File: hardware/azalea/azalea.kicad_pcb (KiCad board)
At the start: 2 copper layers, 73.7 x 55.9 mm, 86 parts, among them J1 NEIGHBOR1, J2 NEIGHBOR2, J3 USB-MICRO-B-SHIELDED, J4 USB-MICRO-B-SHIELDED, J5 JTAG, J6 RTC, J7 BONUS_ROW, SW1 DFU, SW2 RESET, U1 LPC4330FBD144, U2 W25Q16DV, U3 AP7333, U4 IP4220CZ6, U5 NX5P2553GV, X1 XTAL4PIN, X2 RTC_XTAL

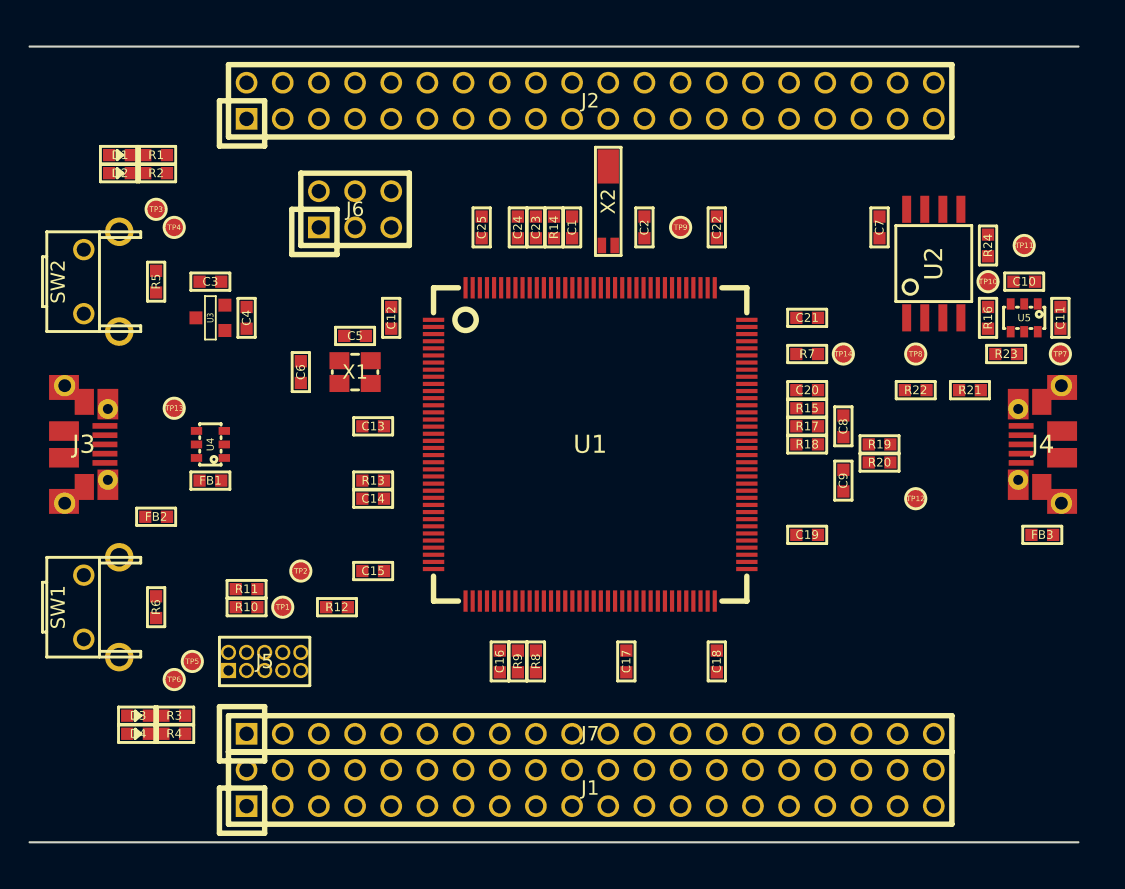
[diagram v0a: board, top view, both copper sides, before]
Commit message: azalea: added mounting holes
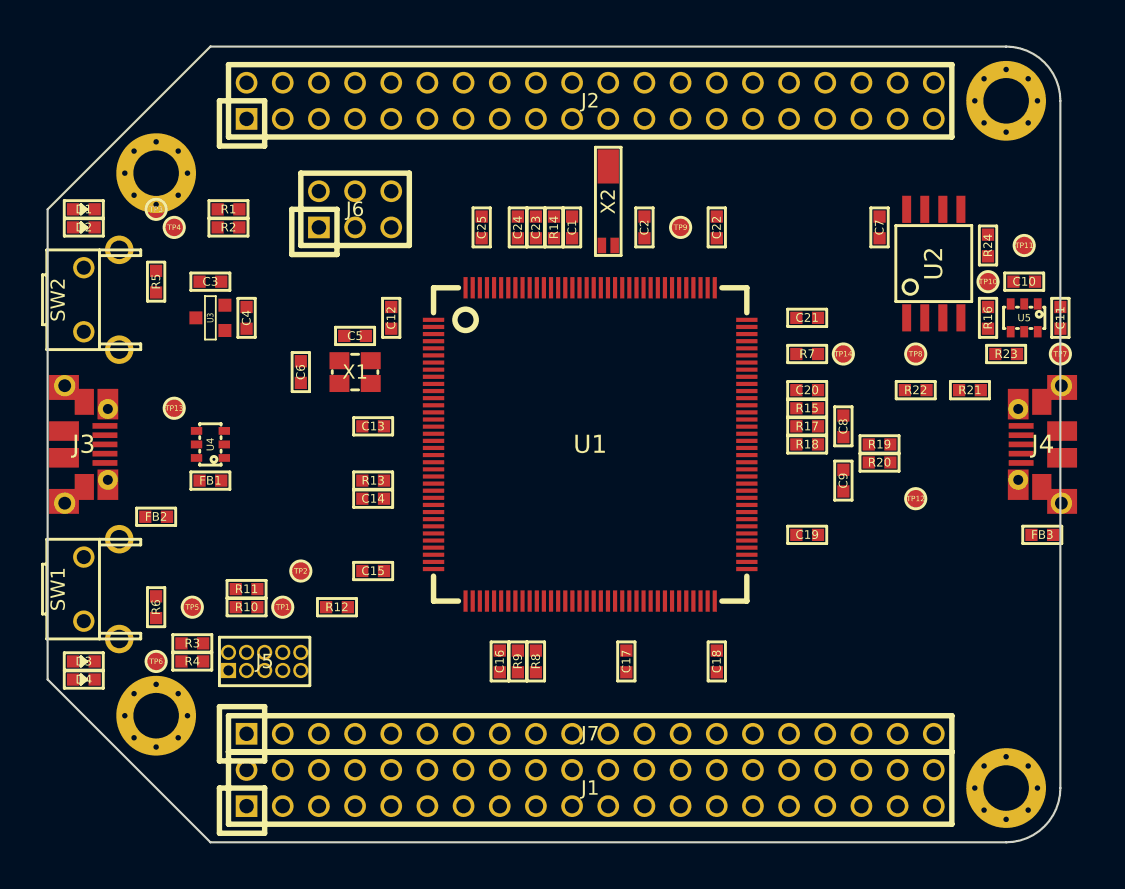
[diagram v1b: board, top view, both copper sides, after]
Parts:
- added MH1: MOUNTING_HOLE, gsg-modules:HOLE126MIL-COPPER, F.Cu at (111.8, 78.7)
- added MH2: MOUNTING_HOLE, gsg-modules:HOLE126MIL-COPPER, F.Cu at (111.8, 116.8)
- added MH3: MOUNTING_HOLE, gsg-modules:HOLE126MIL-COPPER, F.Cu at (171.4, 121.9)
- added MH4: MOUNTING_HOLE, gsg-modules:HOLE126MIL-COPPER, F.Cu at (171.4, 73.7)
- moved R1 6.35 mm to (116.8, 81.3)
- moved R2 6.35 mm to (116.8, 82.5)
- moved D3 5.39 mm to (106.7, 113.0)
- moved D4 5.39 mm to (106.7, 114.3)
- moved R3 5.24 mm to (114.3, 111.8)
- moved R4 5.24 mm to (114.3, 113.0)
- moved D1 4.58 mm to (106.7, 81.3)
- moved D2 4.58 mm to (106.7, 82.5)
- moved TP5 3.81 mm to (114.3, 109.2)
- moved TP6 1.80 mm to (111.8, 113.0)
- moved SW1 1.27 mm to (106.7, 108.0)
- moved SW2 1.27 mm to (106.7, 87.6)
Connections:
- net Net-(R10-Pad2) renamed /DBGEN
- net Net-(TP2-Pad1) renamed /TRST
- C1 pad 1: /RTCX1 -> /RTCX2
- C2 pad 1: /RTCX2 -> /RTCX1
- X2 pad 1: /RTCX1 -> /RTCX2
- X2 pad 2: /RTCX2 -> /RTCX1
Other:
- board size 73.7 x 55.9 mm -> 71.1 x 55.9 mm

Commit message: azalea: PCB shape
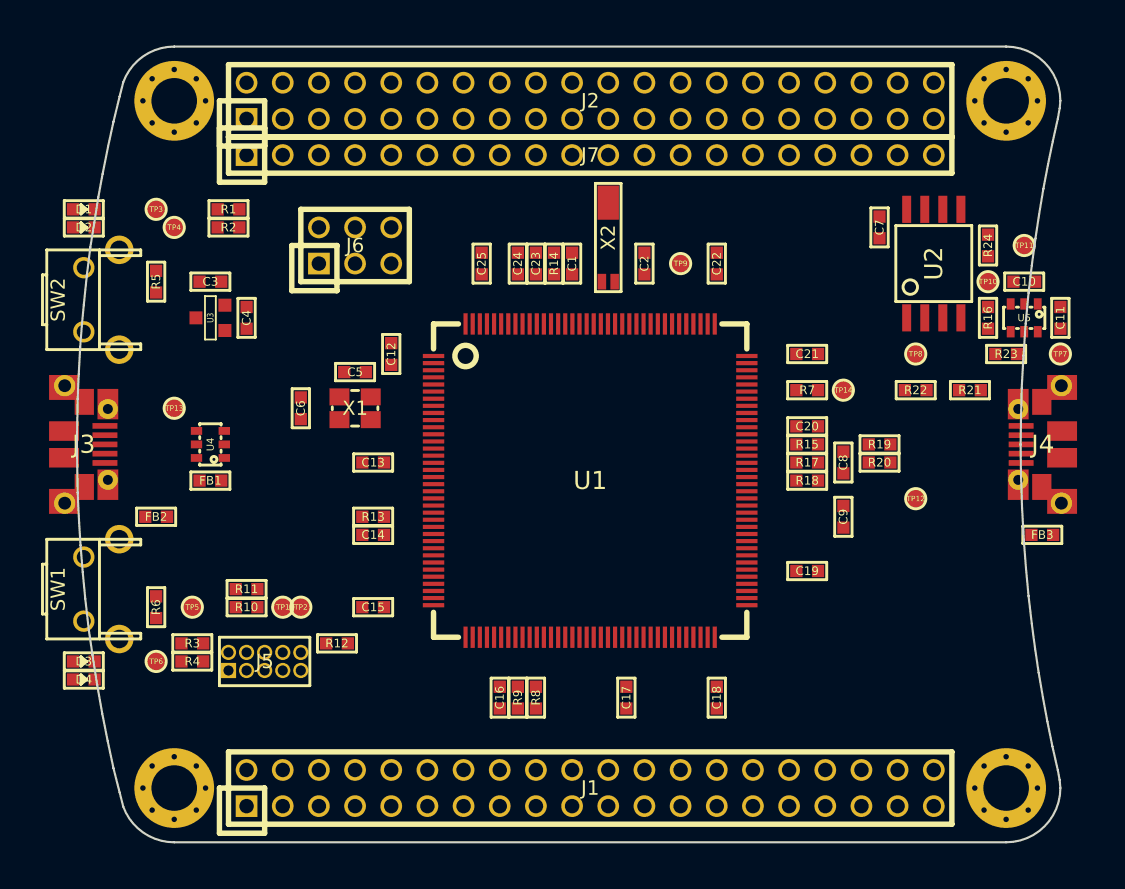
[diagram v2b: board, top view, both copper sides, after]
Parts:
- moved J7 40.6 mm to (142.2, 77.5)
- moved MH1 5.24 mm to (113.0, 73.7)
- moved MH2 5.24 mm to (113.0, 121.9)
- moved C1 2.54 mm to (141.0, 85.1)
- moved C13 2.54 mm to (127.0, 99.1)
- moved C14 2.54 mm to (127.0, 104.1)
- moved C19 2.54 mm to (157.5, 106.7)
- moved C2 2.54 mm to (146.1, 85.1)
- moved C22 2.54 mm to (151.1, 85.1)
- moved C23 2.54 mm to (138.4, 85.1)
- moved C24 2.54 mm to (137.2, 85.1)
- moved C25 2.54 mm to (134.6, 85.1)
- moved C6 2.54 mm to (121.9, 95.2)
- moved C8 2.54 mm to (160.0, 99.1)
- moved C9 2.54 mm to (160.0, 102.9)
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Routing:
- net /P1_10: track 0.00 -> 0.74 mm
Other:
- board size 71.1 x 55.9 mm -> 69.1 x 55.9 mm
- net class Default: clearance 0.2 -> 0.2032; trace_width 0.25 -> 0.2032; via_dia 0.6 -> 0.635; via_drill 0.4 -> 0.381
- rule trace_clearance: 0.2 -> 0.2032
- rule trace_min: 0.2 -> 0.2032
- rule via_min_drill: 0.3 -> 0.2032
- rule via_min_size: 0.4 -> 0.508

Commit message: azalea: made PCB slightly longer and narrower, mounting holes assymmetrical
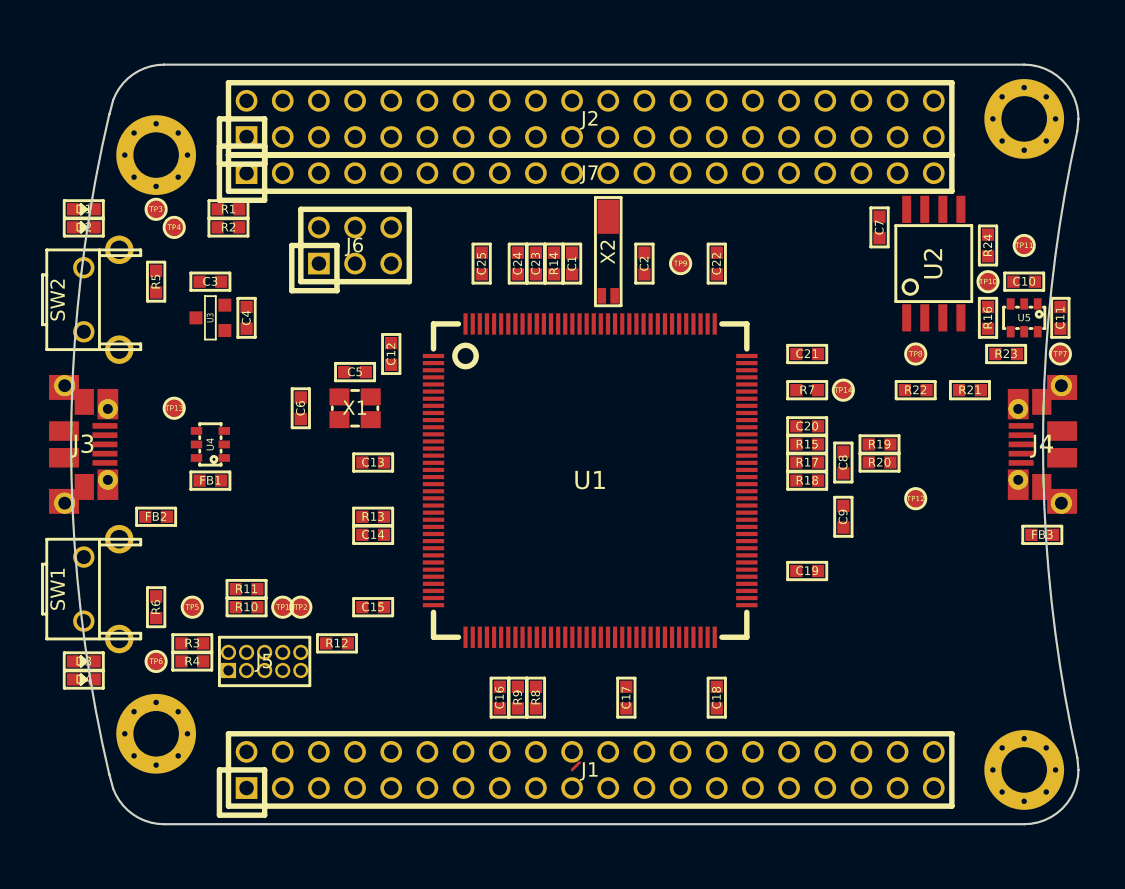
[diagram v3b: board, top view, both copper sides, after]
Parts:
- moved MH1 4.02 mm to (111.8, 77.5)
- moved MH2 4.02 mm to (111.8, 118.1)
- moved MH4 1.80 mm to (172.7, 74.9)
- moved MH3 1.80 mm to (172.7, 120.7)
- moved J2 1.27 mm to (142.2, 74.9)
- moved J1 1.27 mm to (142.2, 120.7)
- moved J7 1.27 mm to (142.2, 78.7)
- moved X2 0.99 mm to (143.5, 87.4)
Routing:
- net /P1_10: track 0.74 -> 0.00 mm
- net (no net): track 0.00 -> 0.74 mm
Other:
- board size 69.1 x 55.9 mm -> 70.7 x 53.3 mm

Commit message: azalea: approximate component placement
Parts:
- moved C7 8.53 mm to (157.5, 89.4), turned to 0 degrees
- moved U2 7.38 mm to (159.0, 85.6), turned to 180 degrees
- moved TP6 6.76 mm to (115.6, 107.4)
- moved R5 4.10 mm to (115.6, 84.8), turned to 180 degrees
- moved R16 2.55 mm to (167.6, 88.6)
- moved TP10 2.55 mm to (167.6, 86.1)
- moved R24 2.55 mm to (167.6, 83.6)
- moved C10 2.55 mm to (170.2, 86.1)
- moved C11 2.55 mm to (172.7, 88.6)
- moved U5 2.55 mm to (170.2, 88.6)
- moved R23 2.55 mm to (168.9, 91.2)
- moved TP11 2.55 mm to (170.2, 83.6)
- moved TP7 2.55 mm to (172.7, 91.2)
- moved FB3 2.54 mm to (171.4, 104.1)
- moved SW1 2.54 mm to (109.2, 108.0)
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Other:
- board text added: "GreatFET Azalea"

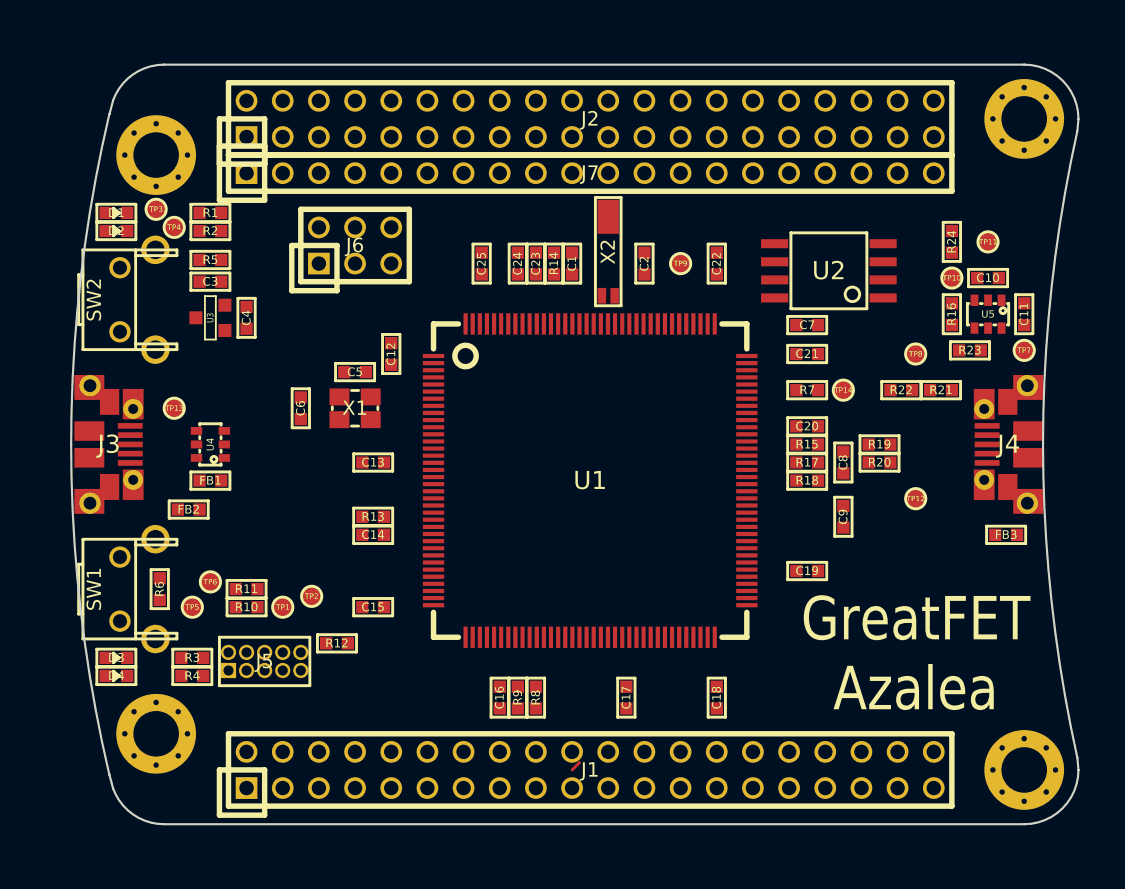
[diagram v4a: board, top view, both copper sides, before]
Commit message: azalea: selected lower profile switch
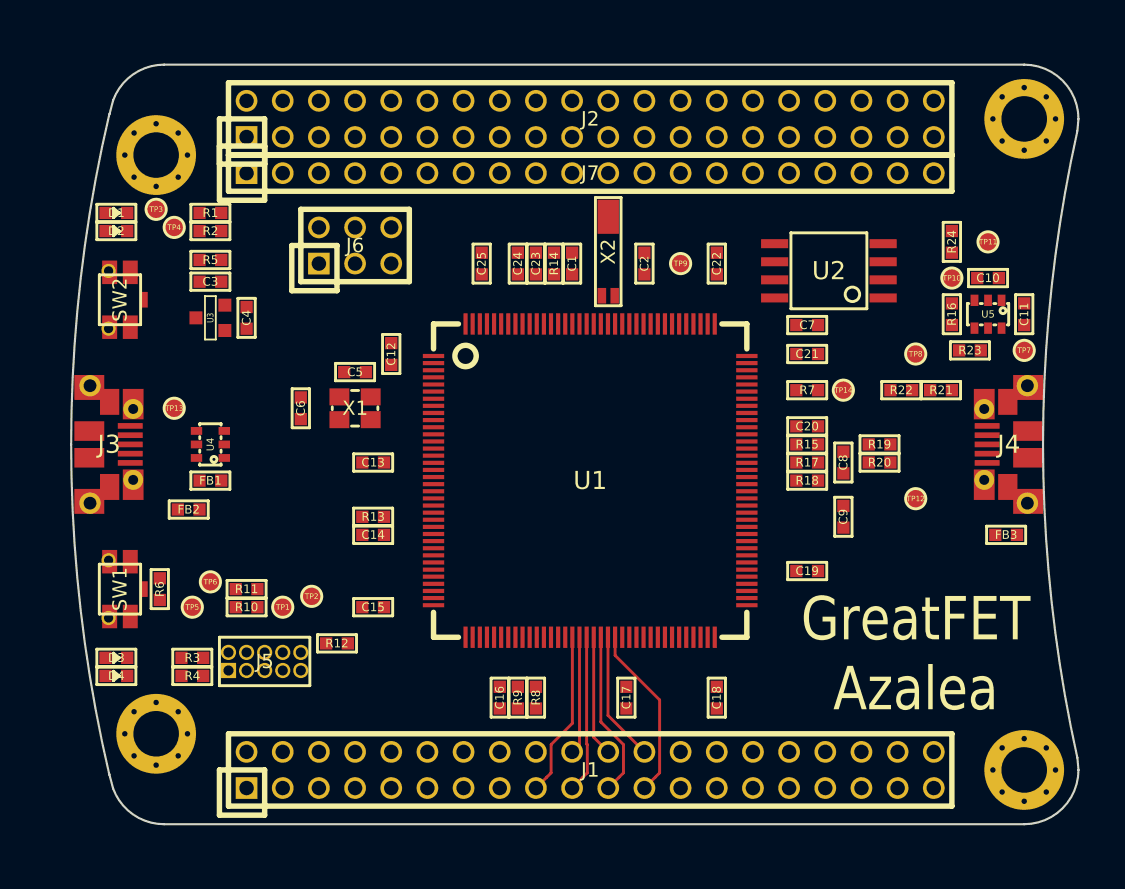
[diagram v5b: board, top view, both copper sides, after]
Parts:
- SW1, SW2: footprint gsg-modules:SWITCH-FSMRA -> gsg-modules:SWITCH-PTS840-P
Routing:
- net /P5_5: track 0.00 -> 12.3 mm
- net /P1_12: track 0.00 -> 11.7 mm
- net /P1_9: track 0.00 -> 11.6 mm
- net /P5_3: track 0.00 -> 11.1 mm
- net /P5_4: track 0.00 -> 9.11 mm
- net /P1_11: track 0.00 -> 8.47 mm
- net /P1_10: track 0.00 -> 8.26 mm
- net (no net): track 0.74 -> 0.00 mm

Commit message: azalea: completed most of the routing
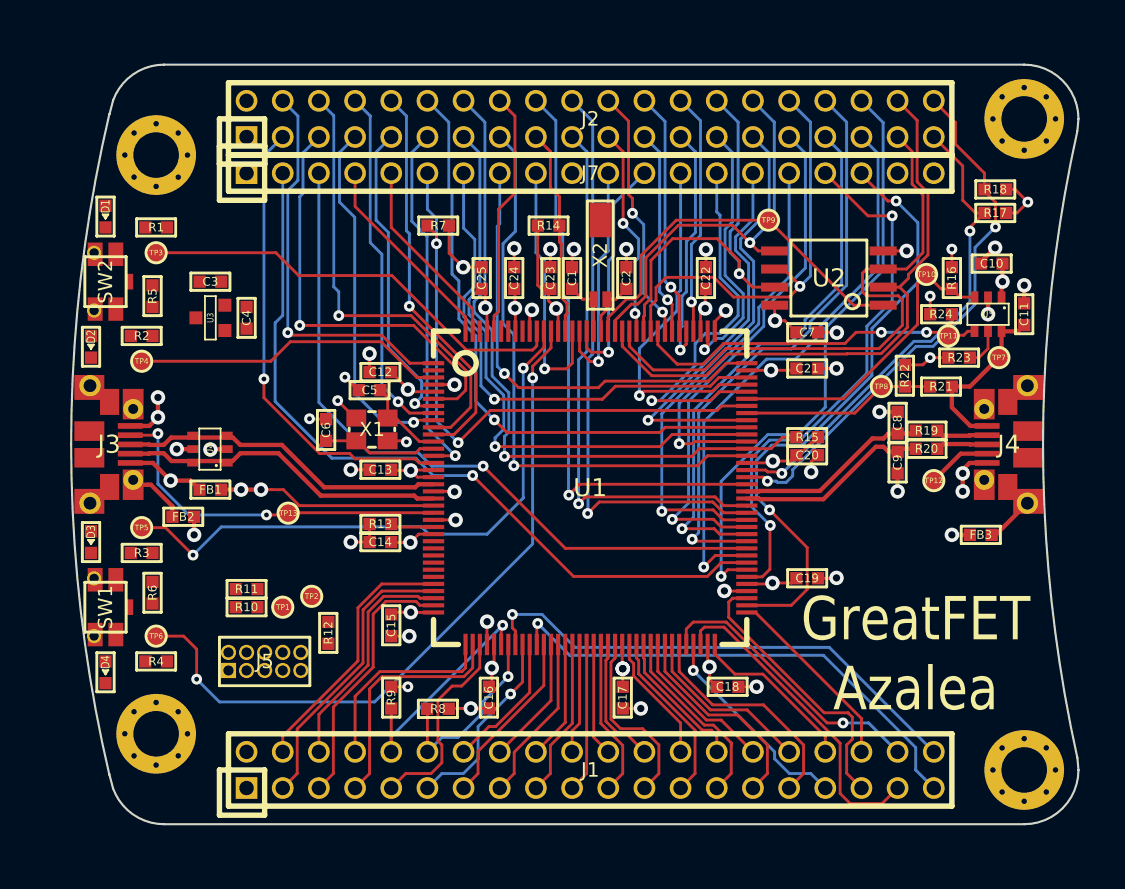
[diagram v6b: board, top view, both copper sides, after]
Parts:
- removed J6: RTC, gsg-modules:HEADER-2x3
- removed TP14: P2_9, gsg-modules:TESTPOINT-50MIL
- moved R7 28.4 mm to (131.6, 82.4), turned to 0 degrees
- moved R18 24.3 mm to (170.7, 79.9), turned to 180 degrees
- moved R17 21.9 mm to (170.7, 81.5), turned to 180 degrees
- moved TP13 10.9 mm to (121.0, 102.6)
- moved TP4 9.67 mm to (110.7, 91.9)
- moved R9 8.89 mm to (128.3, 115.6), turned to 270 degrees
- moved R2 8.81 mm to (110.7, 90.2)
- moved D2 8.32 mm to (107.2, 90.9), turned to 90 degrees
- moved D3 8.32 mm to (107.2, 104.6), turned to 90 degrees
- moved R3 8.18 mm to (110.7, 105.4)
- moved TP11 7.17 mm to (167.4, 90.2)
- moved R8 6.93 mm to (131.5, 116.4), turned to 0 degrees
- moved TP9 6.88 mm to (154.8, 82.0)
- moved TP5 6.62 mm to (110.7, 103.6)
- moved C9 5.39 mm to (163.8, 99.1)
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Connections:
- net Net-(C8-Pad1) renamed /USB1_D-
- net Net-(C9-Pad1) renamed /USB1_D+
- net Net-(J3-Pad2) renamed /USB0_D-
- net Net-(J3-Pad3) renamed /USB0_D+
- J1 pad 10: /P5_1 -> /P1_1
- J1 pad 37: /P1_19 -> /P1_20
- J1 pad 38: /P1_20 -> /P1_19
- J1 pad 39: /P1_3 -> /P1_4
- J1 pad 40: /P1_4 -> /P1_3
- J1 pad 9: /P1_1 -> /P5_1
- J2 pad 10: /ADC0_0 -> /P4_6
- J2 pad 11: /P4_0 -> /P4_7
- J2 pad 12: /P7_7 -> /CLK2
- J2 pad 13: /WAKEUP0 -> /P2_8
- J2 pad 14: /P3_7 -> /P2_7
- J2 pad 15: /P3_6 -> /P2_6
- J2 pad 16: /P3_5 -> /P7_7
- J2 pad 17: /P3_4 -> /WAKEUP0
- J2 pad 18: /P3_3 -> /P2_5
- J2 pad 19: /PF_4 -> /P2_4
- J2 pad 20: /P3_2 -> /P2_3
- J2 pad 21: /P7_2 -> /PF_4
- J2 pad 22: /P3_1 -> /P3_2
- J2 pad 23: /P7_1 -> /P7_2
- J2 pad 24: /P3_0 -> /P3_1
- J2 pad 25: /P7_0 -> /P7_1
- J2 pad 26: /CLK2 -> /P3_0
- J2 pad 27: /P2_8 -> /P7_0
- J2 pad 28: /P2_7 -> /P3_4
- J2 pad 29: /P2_6 -> /P6_8
- J2 pad 30: /P2_5 -> /P3_7
- J2 pad 31: /P2_4 -> /P6_7
- J2 pad 32: /P2_3 -> /P3_3
- J2 pad 33: /P6_8 -> /P2_2
- J2 pad 34: /P6_7 -> /P6_6
- J2 pad 35: /P2_2 -> /P2_1
- J2 pad 36: /P6_6 -> /P6_3
- J2 pad 37: /P2_1 -> /P3_5
- J2 pad 38: /P6_3 -> /P3_6
- J2 pad 4: /P4_7 -> /P4_0
- J2 pad 5: /P4_6 -> /ADC0_0
- J7 pad 10: /P2_12 -> GND
- J7 pad 11: /P2_11 -> /RESET
- J7 pad 12: /P2_10 -> /VBAT
- J7 pad 13: /P2_9 -> /P2_11
- J7 pad 14: /P6_10 -> /P2_10
- J7 pad 15: /P6_9 -> /P6_10
- J7 pad 16: /P6_5 -> /P6_9
- J7 pad 17: /P6_4 -> /P6_2
- J7 pad 18: /P6_2 -> /P6_1
- J7 pad 19: /P6_1 -> GND
- J7 pad 2: /ADC0_1 -> /P6_4
- J7 pad 3: /ADC0_5 -> /P6_5
- J7 pad 4: /ADC0_2 -> /ADC0_5
- J7 pad 5: /ADC0_6 -> /ADC0_2
- J7 pad 6: /ADC0_3 -> /P2_9
- J7 pad 7: /ADC0_4 -> /P2_12
- J7 pad 8: /ADC0_7 -> /P2_13
- J7 pad 9: /P2_13 -> /RTC_ALARM
- U1 pad 132: /LED1 -> /LED4
- U1 pad 133: /LED2 -> /LED3
- U1 pad 134: /LED3 -> /LED1
- U1 pad 136: /ADC0_7 -> Net-(U1-Pad136)
- U1 pad 138: /ADC0_4 -> Net-(U1-Pad138)
- U1 pad 139: /ADC0_3 -> Net-(U1-Pad139)
- U1 pad 142: /ADC0_6 -> Net-(U1-Pad142)
- U1 pad 2: /ADC0_1 -> Net-(U1-Pad2)
- U1 pad 3: /LED4 -> /LED2
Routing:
- net GND: track 0.00 -> 68.5 mm, vias 0 -> 43
- net VCC: track 0.00 -> 63.8 mm, vias 0 -> 19
- net /P6_4: track 0.00 -> 54.9 mm, vias 0 -> 1
- net /P6_5: track 0.00 -> 50.4 mm, vias 0 -> 1
- net /LED4: track 0.00 -> 49.7 mm, vias 0 -> 2
- net /P2_7: track 0.00 -> 48.1 mm, vias 0 -> 1
- net /P6_1: track 0.00 -> 43.4 mm, vias 0 -> 2
- net /P2_9: track 0.00 -> 42.7 mm, vias 0 -> 2
- net /CLK2: track 0.00 -> 42.6 mm, vias 0 -> 1
- net /P3_6: track 0.00 -> 42.3 mm
- net /P3_5: track 0.00 -> 42.0 mm
- net /LED3: track 0.00 -> 42.0 mm, vias 0 -> 2
- net /P6_3: track 0.00 -> 42.0 mm, vias 0 -> 1
- net /P2_8: track 0.00 -> 41.8 mm, vias 0 -> 1
- net /P2_3: track 0.00 -> 41.6 mm, vias 0 -> 1
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- added copper zone on In1.Cu, net GND
- added copper zone on In2.Cu, net VCC
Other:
- copper layers 2 -> 4
- net class Default: clearance 0.2032 -> 0.1524; via_dia 0.635 -> 0.762; via_drill 0.381 -> 0.3302
- rule pad_to_mask_clearance: 0.2 -> 0.127
- rule trace_clearance: 0.2032 -> 0.1524
- rule via_min_drill: 0.2032 -> 0.3302
- rule via_min_size: 0.508 -> 0.6858
